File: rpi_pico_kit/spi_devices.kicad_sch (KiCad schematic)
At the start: 20 parts, among them J6 Conn_01x08_Male, J7 Conn_01x08_Male, J8 Conn_01x08_Male, J9 Micro_SD_Card_Det, SW10 SW_Push, SW7 SW_Push, SW8 SW_Push, SW9 SW_Push, U7 MCP23S08-xSO

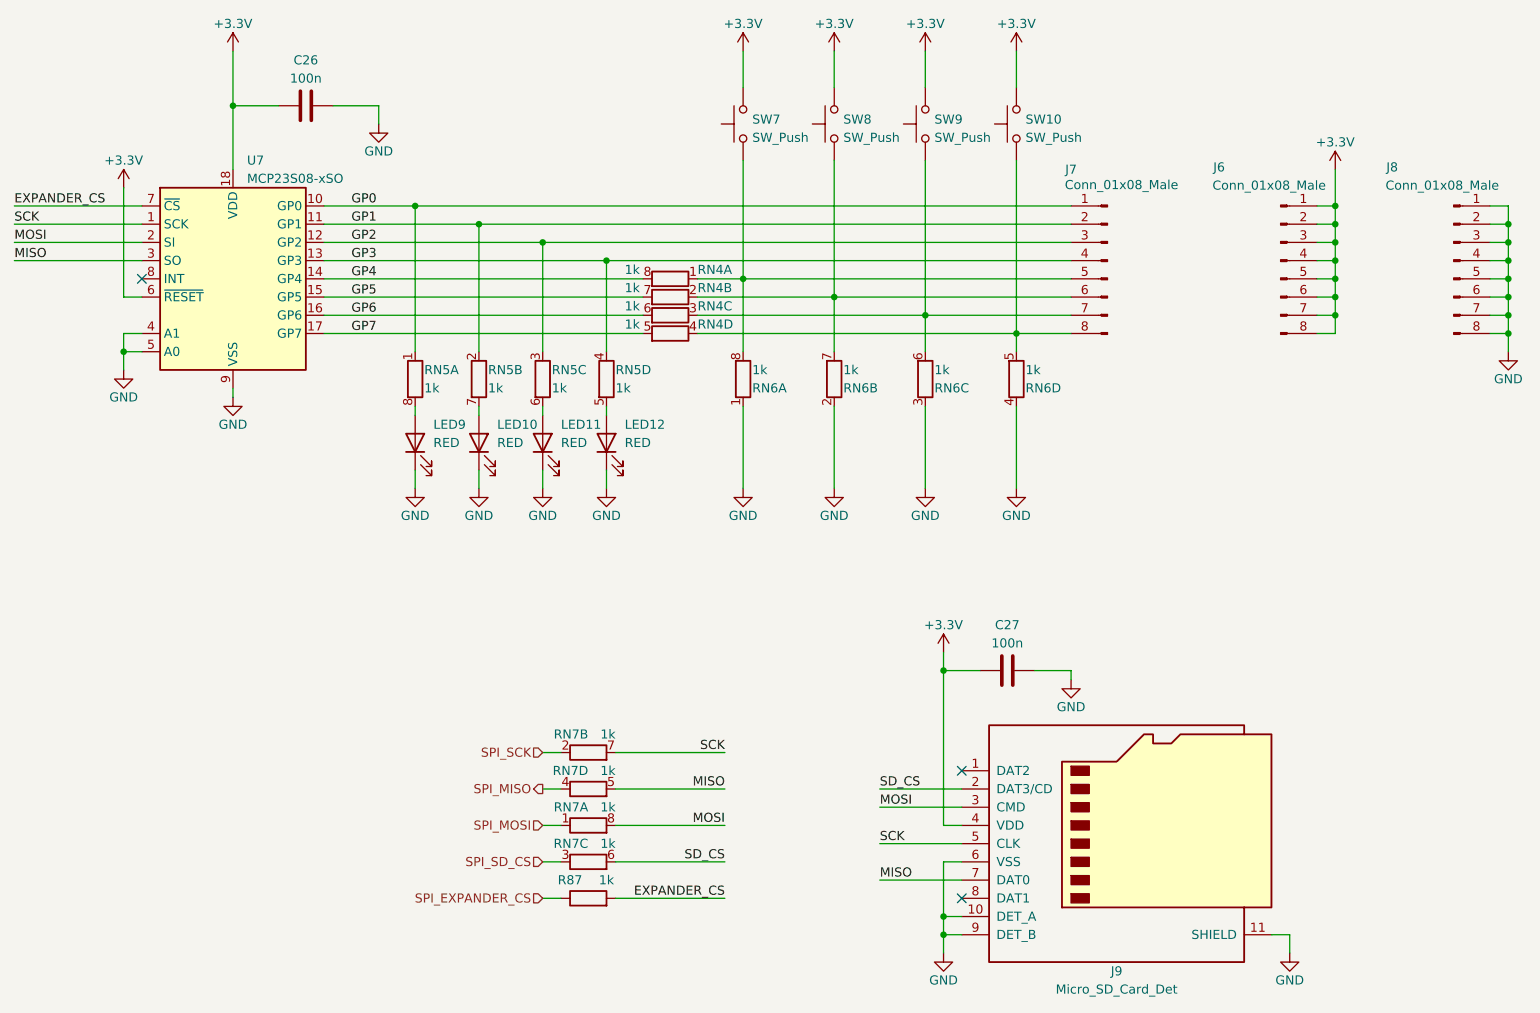
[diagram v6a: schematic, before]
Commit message: schematic cleared annotation
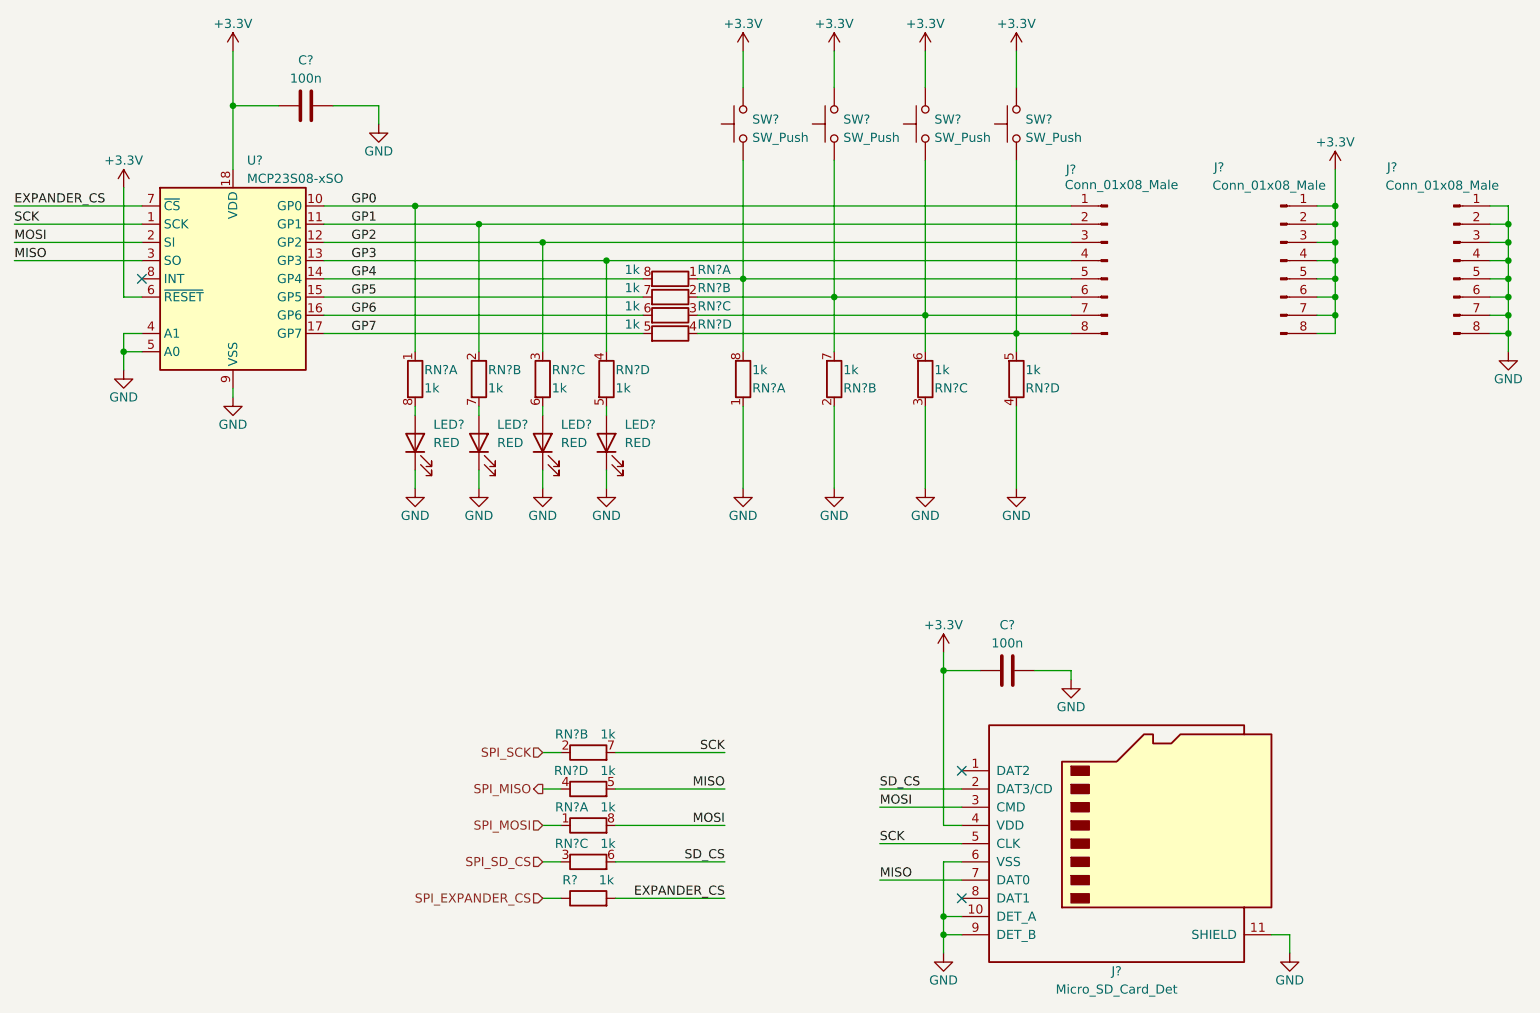
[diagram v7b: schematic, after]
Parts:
- renumbered C26 to C?, C27 to C?, J8 to J?, J7 to J?, J6 to J?, J9 to J?, LED10 to LED?, LED12 to LED?, LED9 to LED?, LED11 to LED?, R87 to R?, RN5 to RN?, RN4 to RN?, RN6 to RN?, RN7 to RN?, SW7 to SW?, SW10 to SW?, SW8 to SW?, SW9 to SW?, U7 to U?

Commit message: renumbered parts
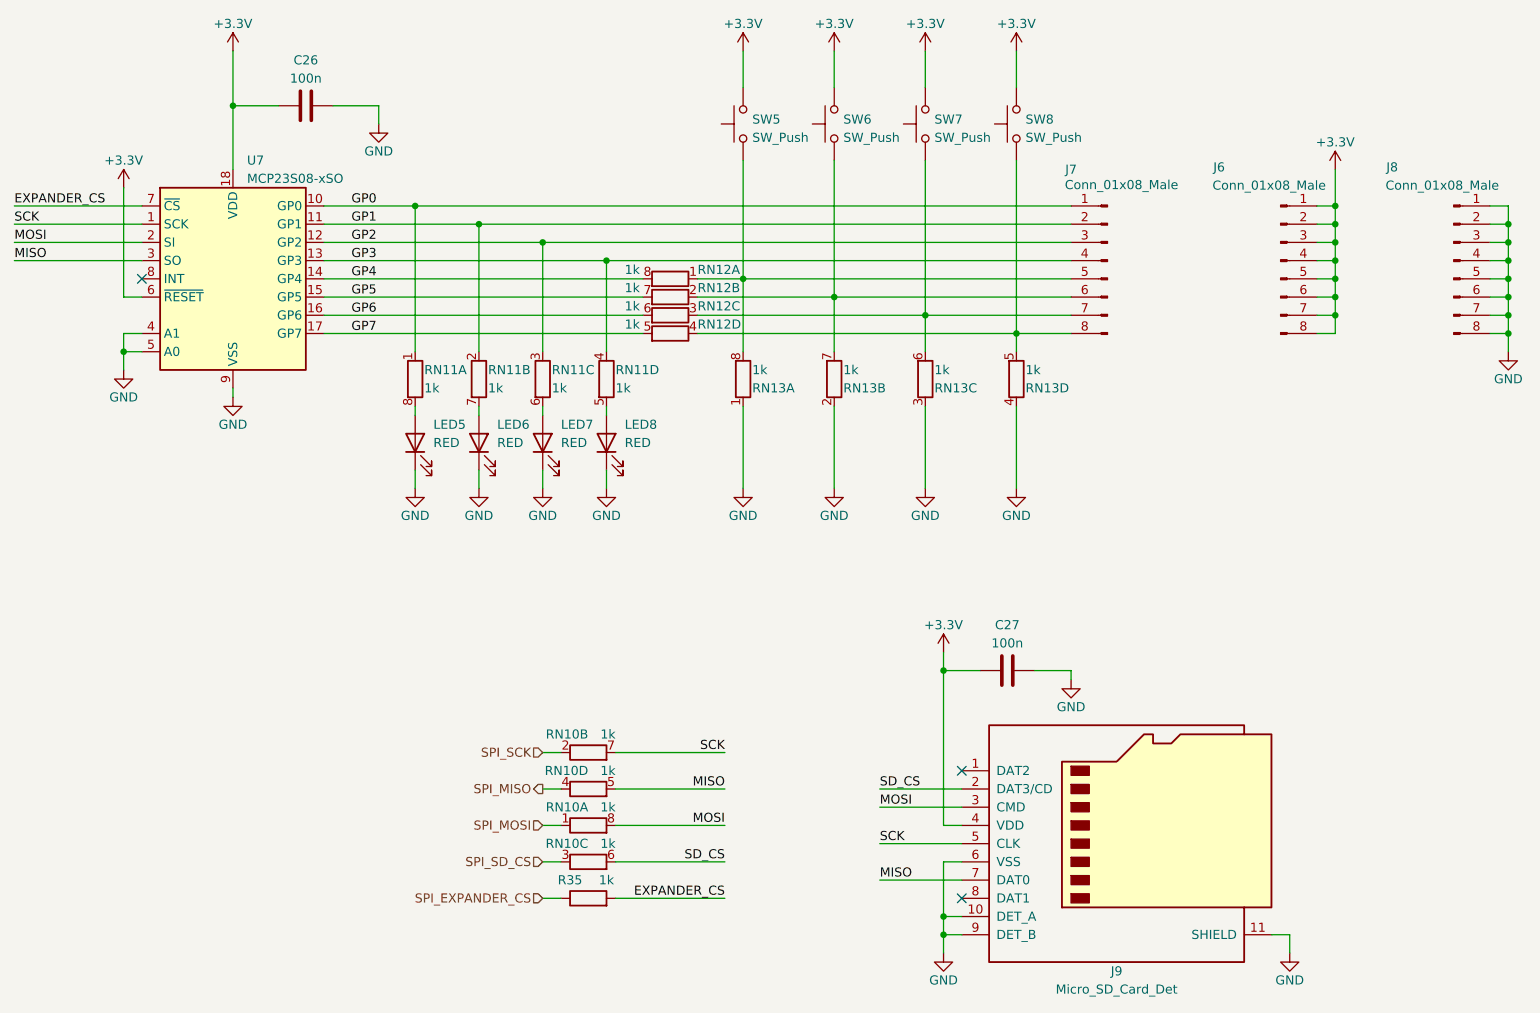
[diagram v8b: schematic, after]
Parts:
- gave numbers to parts that had none: 20
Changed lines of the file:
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@@
   (symbol (lib_id "Device:R") (at 111.76 146.05 90) (unit 1)
     (in_bom yes) (on_board yes)
-    (property "Reference" "R?" (id 0) (at 109.22 143.51 90)
+    (property "Reference" "R35" (id 0) (at 109.22 143.51 90)
       (effects (font (size 1.27 1.27)))
     )
@@
   (symbol (lib_id "Device:LED") (at 96.52 82.55 90) (unit 1)
     (in_bom yes) (on_board yes)
-    (property "Reference" "LED?" (id 0) (at 99.06 80.01 90)
+    (property "Reference" "LED6" (id 0) (at 99.06 80.01 90)
       (effects (font (size 1.27 1.27)) (justify right))
     )
@@
   (symbol (lib_id "Device:R_Pack04_Split") (at 114.3 73.66 180) (unit 4)
     (in_bom yes) (on_board yes)
-    (property "Reference" "RN?" (id 0) (at 115.57 72.39 0)
+    (property "Reference" "RN11" (id 0) (at 115.57 72.39 0)
       (effects (font (size 1.27 1.27)) (justify right))
     )
@@
   (symbol (lib_id "Device:LED") (at 114.3 82.55 90) (unit 1)
     (in_bom yes) (on_board yes)
-    (property "Reference" "LED?" (id 0) (at 116.84 80.01 90)
+    (property "Reference" "LED8" (id 0) (at 116.84 80.01 90)
       (effects (font (size 1.27 1.27)) (justify right))
     )
@@
   (symbol (lib_id "Device:C") (at 72.39 35.56 90) (unit 1)
     (in_bom yes) (on_board yes)
-    (property "Reference" "C?" (id 0) (at 72.39 29.21 90)
+    (property "Reference" "C26" (id 0) (at 72.39 29.21 90)
       (effects (font (size 1.27 1.27)))
     )
@@
   (symbol (lib_id "Device:R_Pack04_Split") (at 123.19 59.69 90) (mirror x) (unit 1)
     (in_bom yes) (on_board yes)
-    (property "Reference" "RN?" (id 0) (at 127 58.42 90)
+    (property "Reference" "RN12" (id 0) (at 127 58.42 90)
       (effects (font (size 1.27 1.27)) (justify right))
     )
@@
   (symbol (lib_id "Connector:Conn_01x08_Male") (at 232.41 57.15 0) (unit 1)
     (in_bom yes) (on_board yes)
-    (property "Reference" "J?" (id 0) (at 223.835 44.1318 0)
+    (property "Reference" "J8" (id 0) (at 223.835 44.1318 0)
       (effects (font (size 1.27 1.27)))
     )
@@
   (symbol (lib_id "Device:R_Pack04_Split") (at 133.35 73.66 0) (mirror y) (unit 1)
     (in_bom yes) (on_board yes)
-    (property "Reference" "RN?" (id 0) (at 134.62 74.93 0)
+    (property "Reference" "RN13" (id 0) (at 134.62 74.93 0)
       (effects (font (size 1.27 1.27)) (justify right))
     )
@@
   (symbol (lib_id "Switch:SW_Push") (at 133.35 38.1 90) (unit 1)
     (in_bom yes) (on_board yes) (fields_autoplaced)
-    (property "Reference" "SW?" (id 0) (at 134.62 37.465 90)
+    (property "Reference" "SW5" (id 0) (at 134.62 37.465 90)
       (effects (font (size 1.27 1.27)) (justify right))
     )
@@
   (symbol (lib_id "Device:R_Pack04_Split") (at 87.63 73.66 180) (unit 1)
     (in_bom yes) (on_board yes)
-    (property "Reference" "RN?" (id 0) (at 88.9 72.39 0)
+    (property "Reference" "RN11" (id 0) (at 88.9 72.39 0)
       (effects (font (size 1.27 1.27)) (justify right))
     )
@@
   (symbol (lib_id "Device:R_Pack04_Split") (at 111.76 125.73 270) (unit 2)
     (in_bom yes) (on_board yes)
-    (property "Reference" "RN?" (id 0) (at 111.76 123.19 90)
+    (property "Reference" "RN10" (id 0) (at 111.76 123.19 90)
       (effects (font (size 1.27 1.27)) (justify right))
     )
@@
   (symbol (lib_id "Device:LED") (at 87.63 82.55 90) (unit 1)
     (in_bom yes) (on_board yes)
-    (property "Reference" "LED?" (id 0) (at 90.17 80.01 90)
+    (property "Reference" "LED5" (id 0) (at 90.17 80.01 90)
       (effects (font (size 1.27 1.27)) (justify right))
     )
@@
   (symbol (lib_id "Device:R_Pack04_Split") (at 123.19 64.77 90) (mirror x) (unit 3)
     (in_bom yes) (on_board yes)
-    (property "Reference" "RN?" (id 0) (at 127 63.5 90)
+    (property "Reference" "RN12" (id 0) (at 127 63.5 90)
       (effects (font (size 1.27 1.27)) (justify right))
     )
@@
   (symbol (lib_id "Device:R_Pack04_Split") (at 111.76 130.81 270) (unit 4)
     (in_bom yes) (on_board yes)
-    (property "Reference" "RN?" (id 0) (at 111.76 128.27 90)
+    (property "Reference" "RN10" (id 0) (at 111.76 128.27 90)
       (effects (font (size 1.27 1.27)) (justify right))
     )
@@
   (symbol (lib_name "MCP23S08-xSO_1") (lib_id "Interface_Expansion:MCP23S08-xSO") (at 62.23 59.69 0) (unit 1)
     (in_bom yes) (on_board yes) (fields_autoplaced)
-    (property "Reference" "U?" (id 0) (at 64.1859 43.18 0)
+    (property "Reference" "U7" (id 0) (at 64.1859 43.18 0)
       (effects (font (size 1.27 1.27)) (justify left))
     )
@@
   (symbol (lib_id "Connector:Conn_01x08_Male") (at 184.15 57.15 0) (mirror y) (unit 1)
     (in_bom yes) (on_board yes)
-    (property "Reference" "J?" (id 0) (at 179.07 44.45 0)
+    (property "Reference" "J7" (id 0) (at 179.07 44.45 0)
       (effects (font (size 1.27 1.27)))
     )
@@
   (symbol (lib_id "Device:R_Pack04_Split") (at 171.45 73.66 0) (mirror y) (unit 4)
     (in_bom yes) (on_board yes)
-    (property "Reference" "RN?" (id 0) (at 172.72 74.93 0)
+    (property "Reference" "RN13" (id 0) (at 172.72 74.93 0)
       (effects (font (size 1.27 1.27)) (justify right))
     )
@@
   (symbol (lib_id "Device:C") (at 170.18 114.3 90) (unit 1)
     (in_bom yes) (on_board yes)
-    (property "Reference" "C?" (id 0) (at 170.18 107.95 90)
+    (property "Reference" "C27" (id 0) (at 170.18 107.95 90)
       (effects (font (size 1.27 1.27)))
     )
@@
   (symbol (lib_id "Connector:Conn_01x08_Male") (at 208.28 57.15 0) (unit 1)
     (in_bom yes) (on_board yes)
-    (property "Reference" "J?" (id 0) (at 199.705 44.1318 0)
+    (property "Reference" "J6" (id 0) (at 199.705 44.1318 0)
       (effects (font (size 1.27 1.27)))
     )
@@
   (symbol (lib_id "Device:R_Pack04_Split") (at 123.19 62.23 90) (mirror x) (unit 2)
     (in_bom yes) (on_board yes)
-    (property "Reference" "RN?" (id 0) (at 127 60.96 90)
+    (property "Reference" "RN12" (id 0) (at 127 60.96 90)
       (effects (font (size 1.27 1.27)) (justify right))
     )
@@
   (symbol (lib_id "Device:R_Pack04_Split") (at 111.76 140.97 270) (unit 3)
     (in_bom yes) (on_board yes)
-    (property "Reference" "RN?" (id 0) (at 111.76 138.43 90)
+    (property "Reference" "RN10" (id 0) (at 111.76 138.43 90)
       (effects (font (size 1.27 1.27)) (justify right))
     )
@@
   (symbol (lib_id "Device:R_Pack04_Split") (at 146.05 73.66 0) (mirror y) (unit 2)
     (in_bom yes) (on_board yes)
-    (property "Reference" "RN?" (id 0) (at 147.32 74.93 0)
+    (property "Reference" "RN13" (id 0) (at 147.32 74.93 0)
       (effects (font (size 1.27 1.27)) (justify right))
     )
@@
   (symbol (lib_id "Device:LED") (at 105.41 82.55 90) (unit 1)
     (in_bom yes) (on_board yes)
-    (property "Reference" "LED?" (id 0) (at 107.95 80.01 90)
+    (property "Reference" "LED7" (id 0) (at 107.95 80.01 90)
       (effects (font (size 1.27 1.27)) (justify right))
     )
@@
   (symbol (lib_id "Switch:SW_Push") (at 171.45 38.1 90) (unit 1)
     (in_bom yes) (on_board yes) (fields_autoplaced)
-    (property "Reference" "SW?" (id 0) (at 172.72 37.465 90)
+    (property "Reference" "SW8" (id 0) (at 172.72 37.465 90)
       (effects (font (size 1.27 1.27)) (justify right))
     )
@@
   (symbol (lib_id "Device:R_Pack04_Split") (at 96.52 73.66 180) (unit 2)
     (in_bom yes) (on_board yes)
-    (property "Reference" "RN?" (id 0) (at 97.79 72.39 0)
+    (property "Reference" "RN11" (id 0) (at 97.79 72.39 0)
       (effects (font (size 1.27 1.27)) (justify right))
     )
@@
   (symbol (lib_id "Connector:Micro_SD_Card_Det") (at 186.69 138.43 0) (unit 1)
     (in_bom yes) (on_board yes)
-    (property "Reference" "J?" (id 0) (at 185.42 156.21 0)
+    (property "Reference" "J9" (id 0) (at 185.42 156.21 0)
       (effects (font (size 1.27 1.27)))
     )
@@
   (symbol (lib_id "Device:R_Pack04_Split") (at 105.41 73.66 180) (unit 3)
     (in_bom yes) (on_board yes)
-    (property "Reference" "RN?" (id 0) (at 106.68 72.39 0)
+    (property "Reference" "RN11" (id 0) (at 106.68 72.39 0)
       (effects (font (size 1.27 1.27)) (justify right))
     )
@@
   (symbol (lib_id "Switch:SW_Push") (at 146.05 38.1 90) (unit 1)
     (in_bom yes) (on_board yes) (fields_autoplaced)
-    (property "Reference" "SW?" (id 0) (at 147.32 37.465 90)
+    (property "Reference" "SW6" (id 0) (at 147.32 37.465 90)
       (effects (font (size 1.27 1.27)) (justify right))
     )
@@
   (symbol (lib_id "Device:R_Pack04_Split") (at 111.76 135.89 270) (unit 1)
     (in_bom yes) (on_board yes)
-    (property "Reference" "RN?" (id 0) (at 111.76 133.35 90)
+    (property "Reference" "RN10" (id 0) (at 111.76 133.35 90)
       (effects (font (size 1.27 1.27)) (justify right))
     )
@@
   (symbol (lib_id "Device:R_Pack04_Split") (at 123.19 67.31 90) (mirror x) (unit 4)
     (in_bom yes) (on_board yes)
-    (property "Reference" "RN?" (id 0) (at 127 66.04 90)
+    (property "Reference" "RN12" (id 0) (at 127 66.04 90)
       (effects (font (size 1.27 1.27)) (justify right))
     )
@@
   (symbol (lib_id "Switch:SW_Push") (at 158.75 38.1 90) (unit 1)
     (in_bom yes) (on_board yes) (fields_autoplaced)
-    (property "Reference" "SW?" (id 0) (at 160.02 37.465 90)
+    (property "Reference" "SW7" (id 0) (at 160.02 37.465 90)
       (effects (font (size 1.27 1.27)) (justify right))
     )
@@
   (symbol (lib_id "Device:R_Pack04_Split") (at 158.75 73.66 0) (mirror y) (unit 3)
     (in_bom yes) (on_board yes)
-    (property "Reference" "RN?" (id 0) (at 160.02 74.93 0)
-      (effects (font (size 1.27 1.27)) (justify right))
-    )
+    (property "Reference" "RN13" (id 0) (at 160.02 74.93 0)
+      (effects (font (size 1.27 1.27)) (justify right))
+    )
